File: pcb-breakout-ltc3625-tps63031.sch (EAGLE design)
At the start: 16 parts, among them IC1 LTC3625

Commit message: corrected package error in ltc3625 lbr
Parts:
- IC1: value LTC3625 -> LTC3625EDE; device ltc3625:LTC3625 -> ltc3625:LTC3625EDE
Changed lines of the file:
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@@
 </classes>
 <parts>
-<part name="IC1" library="ltc3625" deviceset="LTC3625" device=""/>
+<part name="IC1" library="ltc3625" deviceset="LTC3625" device="EDE"/>
 <part name="JP1" library="pinhead" deviceset="PINHD-1X8" device=""/>
 <part name="JP2" library="pinhead" deviceset="PINHD-1X8" device=""/>

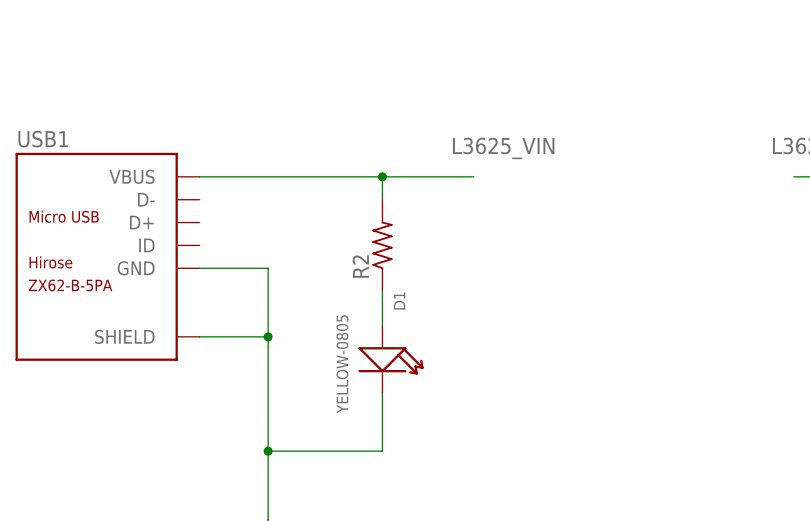
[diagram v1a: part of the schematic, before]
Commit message: 2kohm for led resistor value
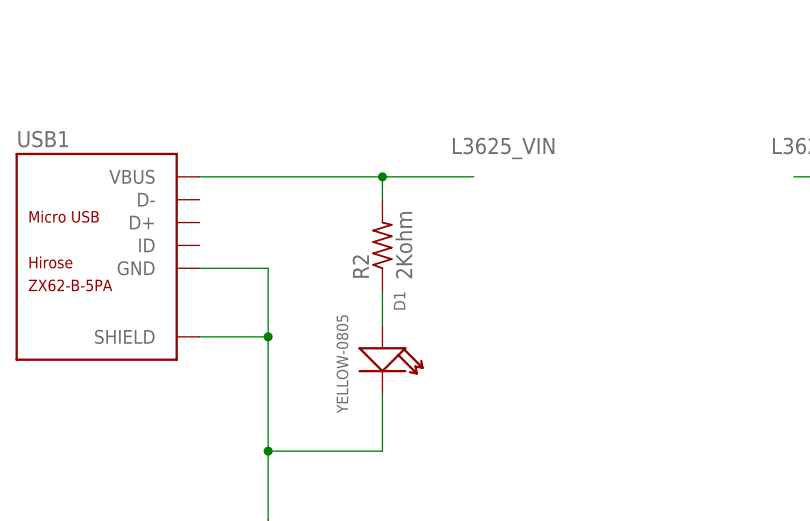
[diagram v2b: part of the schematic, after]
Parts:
- R2: value (none) -> 2Kohm
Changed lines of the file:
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@@
 <grid distance="0.1" unitdist="inch" unit="inch" style="lines" multiple="1" display="no" altdistance="0.01" altunitdist="inch" altunit="inch"/>
 <layers>
-<layer number="1" name="Top" color="4" fill="1" visible="no" active="no"/>
-<layer number="2" name="Route2" color="1" fill="3" visible="no" active="no"/>
-<layer number="3" name="Route3" color="4" fill="3" visible="no" active="no"/>
-<layer number="14" name="Route14" color="1" fill="6" visible="no" active="no"/>
-<layer number="15" name="Route15" color="4" fill="6" visible="no" active="no"/>
-<layer number="16" name="Bottom" color="1" fill="1" visible="no" active="no"/>
-<layer number="17" name="Pads" color="2" fill="1" visible="no" active="no"/>
-<layer number="18" name="Vias" color="2" fill="1" visible="no" active="no"/>
-<layer number="19" name="Unrouted" color="6" fill="1" visible="no" active="no"/>
-<layer number="20" name="Dimension" color="15" fill="1" visible="no" active="no"/>
-<layer number="21" name="tPlace" color="7" fill="1" visible="no" active="no"/>
-<layer number="22" name="bPlace" color="7" fill="1" visible="no" active="no"/>
-<layer number="23" name="tOrigins" color="15" fill="1" visible="no" active="no"/>
-<layer number="24" name="bOrigins" color="15" fill="1" visible="no" active="no"/>
-<layer number="25" name="tNames" color="7" fill="1" visible="no" active="no"/>
-<layer number="26" name="bNames" color="7" fill="1" visible="no" active="no"/>
-<layer number="27" name="tValues" color="7" fill="1" visible="no" active="no"/>
-<layer number="28" name="bValues" color="7" fill="1" visible="no" active="no"/>
+<layer number="1" name="Top" color="4" fill="1" visible="yes" active="no"/>
+<layer number="2" name="Route2" color="1" fill="3" visible="yes" active="no"/>
+<layer number="3" name="Route3" color="4" fill="3" visible="yes" active="no"/>
+<layer number="14" name="Route14" color="1" fill="6" visible="yes" active="no"/>
+<layer number="15" name="Route15" color="4" fill="6" visible="yes" active="no"/>
+<layer number="16" name="Bottom" color="1" fill="1" visible="yes" active="no"/>
+<layer number="17" name="Pads" color="2" fill="1" visible="yes" active="no"/>
+<layer number="18" name="Vias" color="2" fill="1" visible="yes" active="no"/>
+<layer number="19" name="Unrouted" color="6" fill="1" visible="yes" active="no"/>
+<layer number="20" name="Dimension" color="15" fill="1" visible="yes" active="no"/>
+<layer number="21" name="tPlace" color="7" fill="1" visible="yes" active="no"/>
+<layer number="22" name="bPlace" color="7" fill="1" visible="yes" active="no"/>
+<layer number="23" name="tOrigins" color="15" fill="1" visible="yes" active="no"/>
+<layer number="24" name="bOrigins" color="15" fill="1" visible="yes" active="no"/>
+<layer number="25" name="tNames" color="7" fill="1" visible="yes" active="no"/>
+<layer number="26" name="bNames" color="7" fill="1" visible="yes" active="no"/>
+<layer number="27" name="tValues" color="7" fill="1" visible="yes" active="no"/>
+<layer number="28" name="bValues" color="7" fill="1" visible="yes" active="no"/>
 <layer number="29" name="tStop" color="7" fill="3" visible="no" active="no"/>
 <layer number="30" name="bStop" color="7" fill="6" visible="no" active="no"/>
@@
 <layer number="35" name="tGlue" color="7" fill="4" visible="no" active="no"/>
 <layer number="36" name="bGlue" color="7" fill="5" visible="no" active="no"/>
-<layer number="37" name="tTest" color="7" fill="1" visible="no" active="no"/>
-<layer number="38" name="bTest" color="7" fill="1" visible="no" active="no"/>
+<layer number="37" name="tTest" color="7" fill="1" visible="yes" active="no"/>
+<layer number="38" name="bTest" color="7" fill="1" visible="yes" active="no"/>
 <layer number="39" name="tKeepout" color="4" fill="11" visible="no" active="no"/>
 <layer number="40" name="bKeepout" color="1" fill="11" visible="no" active="no"/>
@@
 <layer number="44" name="Drills" color="7" fill="1" visible="no" active="no"/>
 <layer number="45" name="Holes" color="7" fill="1" visible="no" active="no"/>
-<layer number="46" name="Milling" color="3" fill="1" visible="no" active="no"/>
-<layer number="47" name="Measures" color="7" fill="1" visible="no" active="no"/>
-<layer number="48" name="Document" color="7" fill="1" visible="no" active="no"/>
-<layer number="49" name="Reference" color="7" fill="1" visible="no" active="no"/>
-<layer number="50" name="dxf" color="7" fill="1" visible="no" active="no"/>
-<layer number="51" name="tDocu" color="7" fill="1" visible="no" active="no"/>
-<layer number="52" name="bDocu" color="7" fill="1" visible="no" active="no"/>
-<layer number="53" name="tGND_GNDA" color="7" fill="9" visible="no" active="no"/>
-<layer number="54" name="bGND_GNDA" color="1" fill="9" visible="no" active="no"/>
-<layer number="56" name="wert" color="3" fill="1" visible="no" active="no"/>
-<layer number="57" name="tCAD" color="7" fill="1" visible="no" active="no"/>
-<layer number="59" name="tCarbon" color="7" fill="1" visible="no" active="no"/>
-<layer number="60" name="bCarbon" color="7" fill="1" visible="no" active="no"/>
+<layer number="46" name="Milling" color="3" fill="1" visible="yes" active="no"/>
+<layer number="47" name="Measures" color="7" fill="1" visible="yes" active="no"/>
+<layer number="48" name="Document" color="7" fill="1" visible="yes" active="no"/>
+<layer number="49" name="Reference" color="7" fill="1" visible="yes" active="no"/>
+<layer number="50" name="dxf" color="7" fill="1" visible="yes" active="no"/>
+<layer number="51" name="tDocu" color="7" fill="1" visible="yes" active="no"/>
+<layer number="52" name="bDocu" color="7" fill="1" visible="yes" active="no"/>
+<layer number="53" name="tGND_GNDA" color="7" fill="9" visible="yes" active="no"/>
+<layer number="54" name="bGND_GNDA" color="1" fill="9" visible="yes" active="no"/>
+<layer number="56" name="wert" color="3" fill="1" visible="yes" active="no"/>
+<layer number="57" name="tCAD" color="7" fill="1" visible="yes" active="no"/>
+<layer number="59" name="tCarbon" color="7" fill="1" visible="yes" active="no"/>
+<layer number="60" name="bCarbon" color="7" fill="1" visible="yes" active="no"/>
 <layer number="90" name="Modules" color="5" fill="1" visible="yes" active="yes"/>
 <layer number="91" name="Nets" color="2" fill="1" visible="yes" active="yes"/>
@@
 <part name="SUPPLY5" library="supply2" deviceset="GND" device=""/>
 <part name="SUPPLY6" library="supply2" deviceset="GND" device=""/>
-<part name="R2" library="resistor" deviceset="R-US_" device="R0805"/>
+<part name="R2" library="resistor" deviceset="R-US_" device="R0805" value="2Kohm"/>
 <part name="D1" library="Seeed-OPL-Diode" deviceset="SMD-LED-CLEAR-YELLOW(0805)" device="" value="YELLOW-0805"/>
 </parts>

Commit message: Breakout pins TPS EN and PS and add pull up resistors to them
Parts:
- added R3, R4: 10kohm, resistor:R-US_R0805
- JP1, JP2: device pinhead:PINHD-1X8 -> pinhead:PINHD-1X9
- R2: value 2Kohm -> 2kohm
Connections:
- new net TPS63031_EN: JP2.1, R4.1, U$1.EN
- new net TPS63031_PS: JP2.2, R3.1, U$1.PS/SYNC
- net GND: now also JP1.9; no longer JP1.8
- net L3625_PFI: now also JP2.3; no longer JP2.2
- net L3625_PFO: now also JP2.4; no longer JP2.3
- net L3625_PGOOD: now also JP2.5; no longer JP2.4
- net L3625_SW2: now also JP2.8; no longer JP2.7
- net L3625_SW2_IND: now also JP2.9; no longer JP2.8
- net L3625_VMID: now also JP2.6; no longer JP2.5
- net L3625_VOUT: now also JP2.7; no longer JP2.6
- net N$5: now also R3.2, R4.2; no longer U$1.EN, U$1.PS/SYNC
- net TPS63031_VOUT: now also JP1.8; no longer JP2.1
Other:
- moved on the sheet: C2, C3, C4, C5, L3, U$1
